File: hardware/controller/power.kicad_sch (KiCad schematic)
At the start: 17 parts, among them J11 Barrel_Jack, J7 Conn_01x04_Pin, J8 Conn_01x04_Pin, U5 TPS2121RUXR, U8 AP63203WU

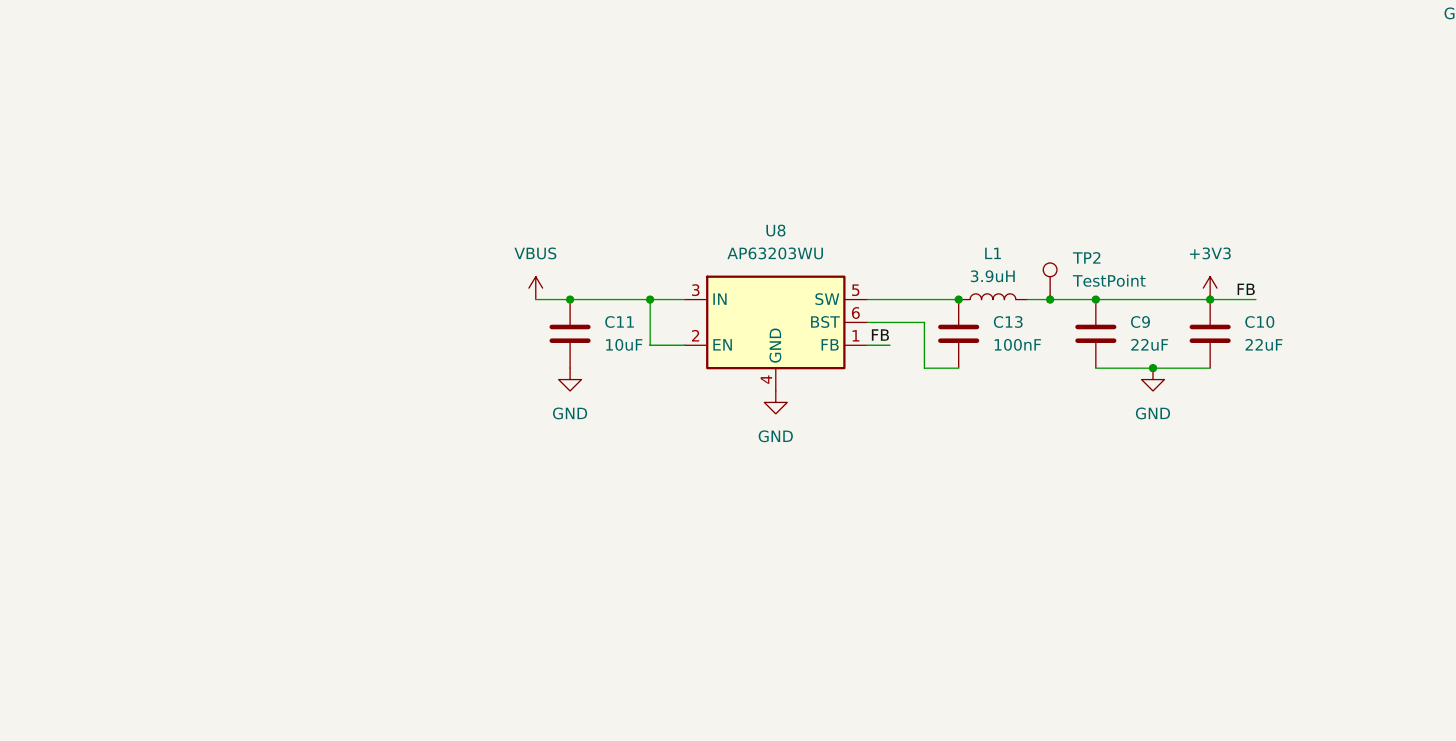
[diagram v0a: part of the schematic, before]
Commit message: Add linear regulator for MAX chips
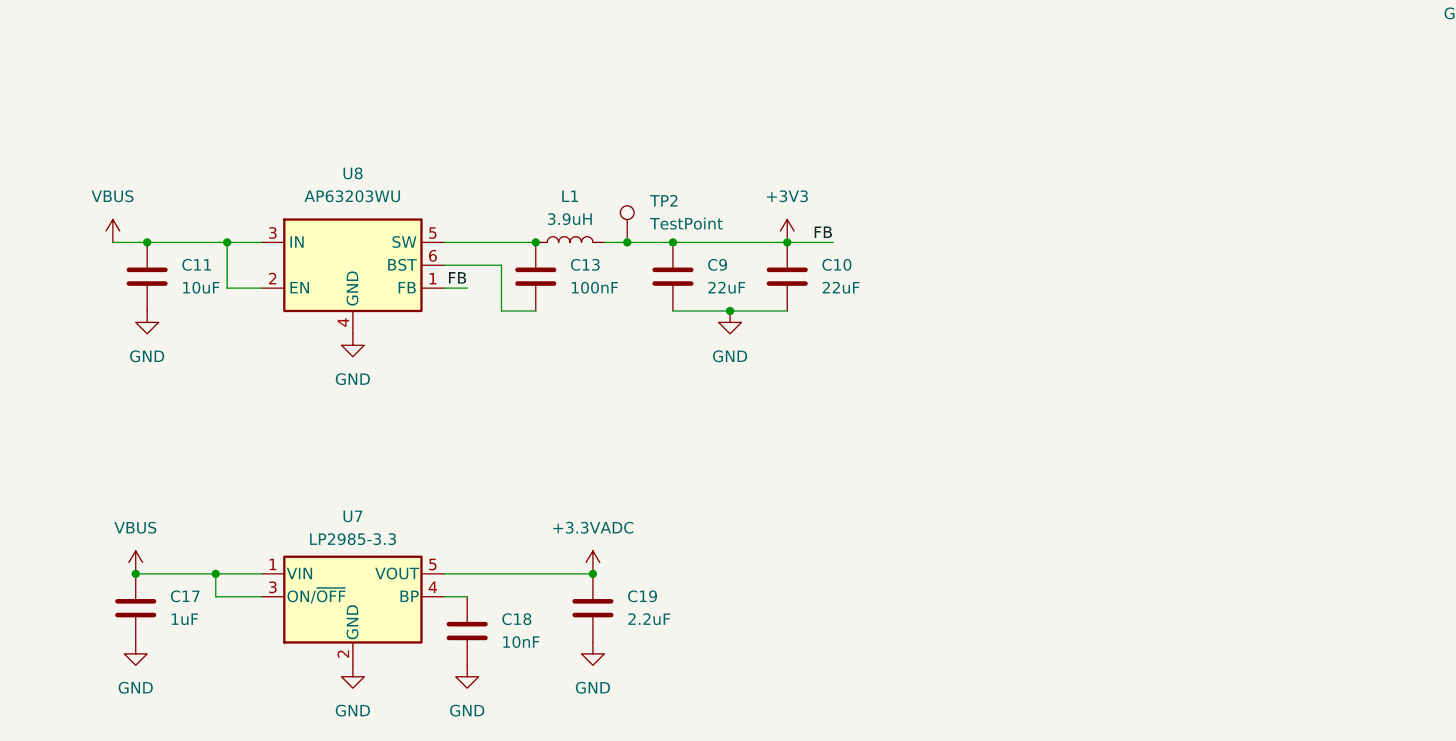
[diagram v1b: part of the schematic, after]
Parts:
- added C17: 1uF, Capacitor_SMD:C_0805_2012Metric, symbol Device:C
- added C18: 10nF, Capacitor_SMD:C_0805_2012Metric, symbol Device:C
- added C19: 2.2uF, Capacitor_SMD:C_0805_2012Metric, symbol Device:C
- added U7: LP2985-3.3, Package_TO_SOT_SMD:SOT-23-5, symbol Regulator_Linear:LP2985-3.3
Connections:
- net GND: now also C17.2, C18.2, C19.2, U7.2 (GND)
- net VBUS: now also C17.1, U7.1 (VIN), U7.3 (ON/~{OFF})
- new net: C18.1, U7.4 (BP)
- new net +3.3VADC: C19.1, U7.5 (VOUT)
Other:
- moved on the sheet: C10, C11, C13, C9, L1, TP2, U8
